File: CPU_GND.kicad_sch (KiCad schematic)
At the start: 1 part

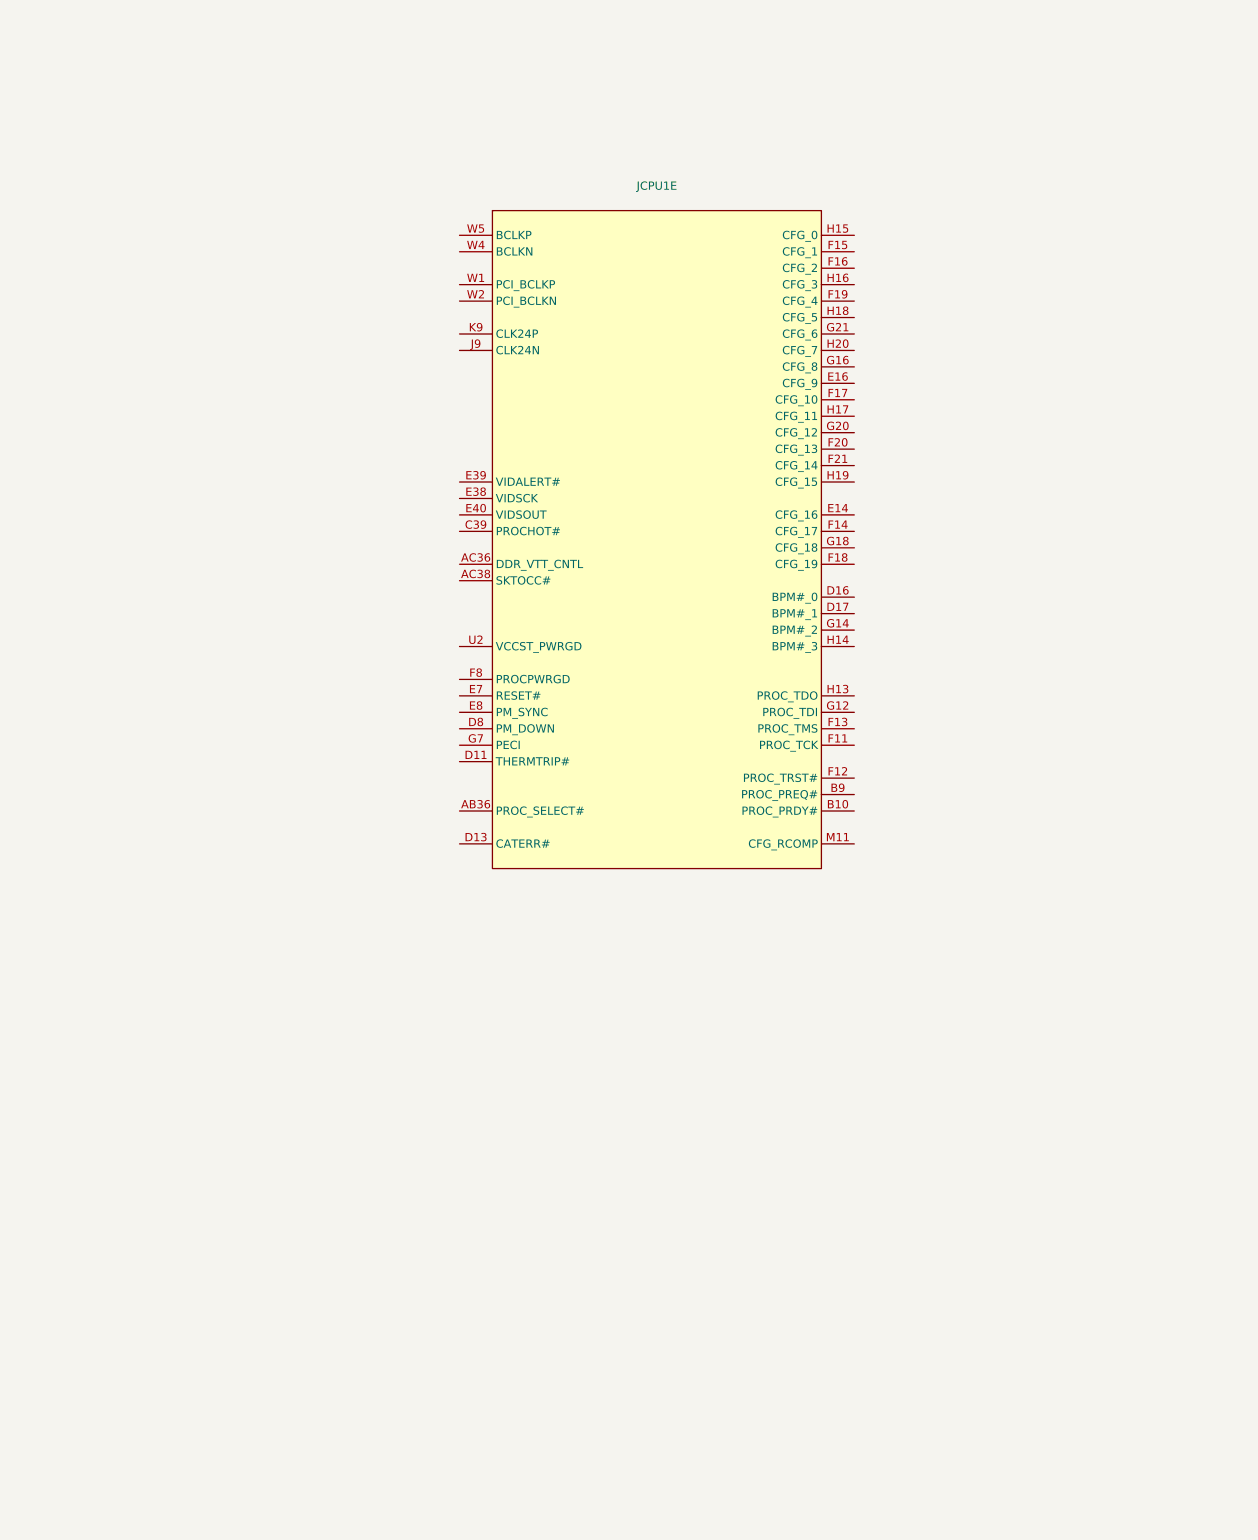
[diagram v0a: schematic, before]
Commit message: Added CPU GND and Core VCC symbols
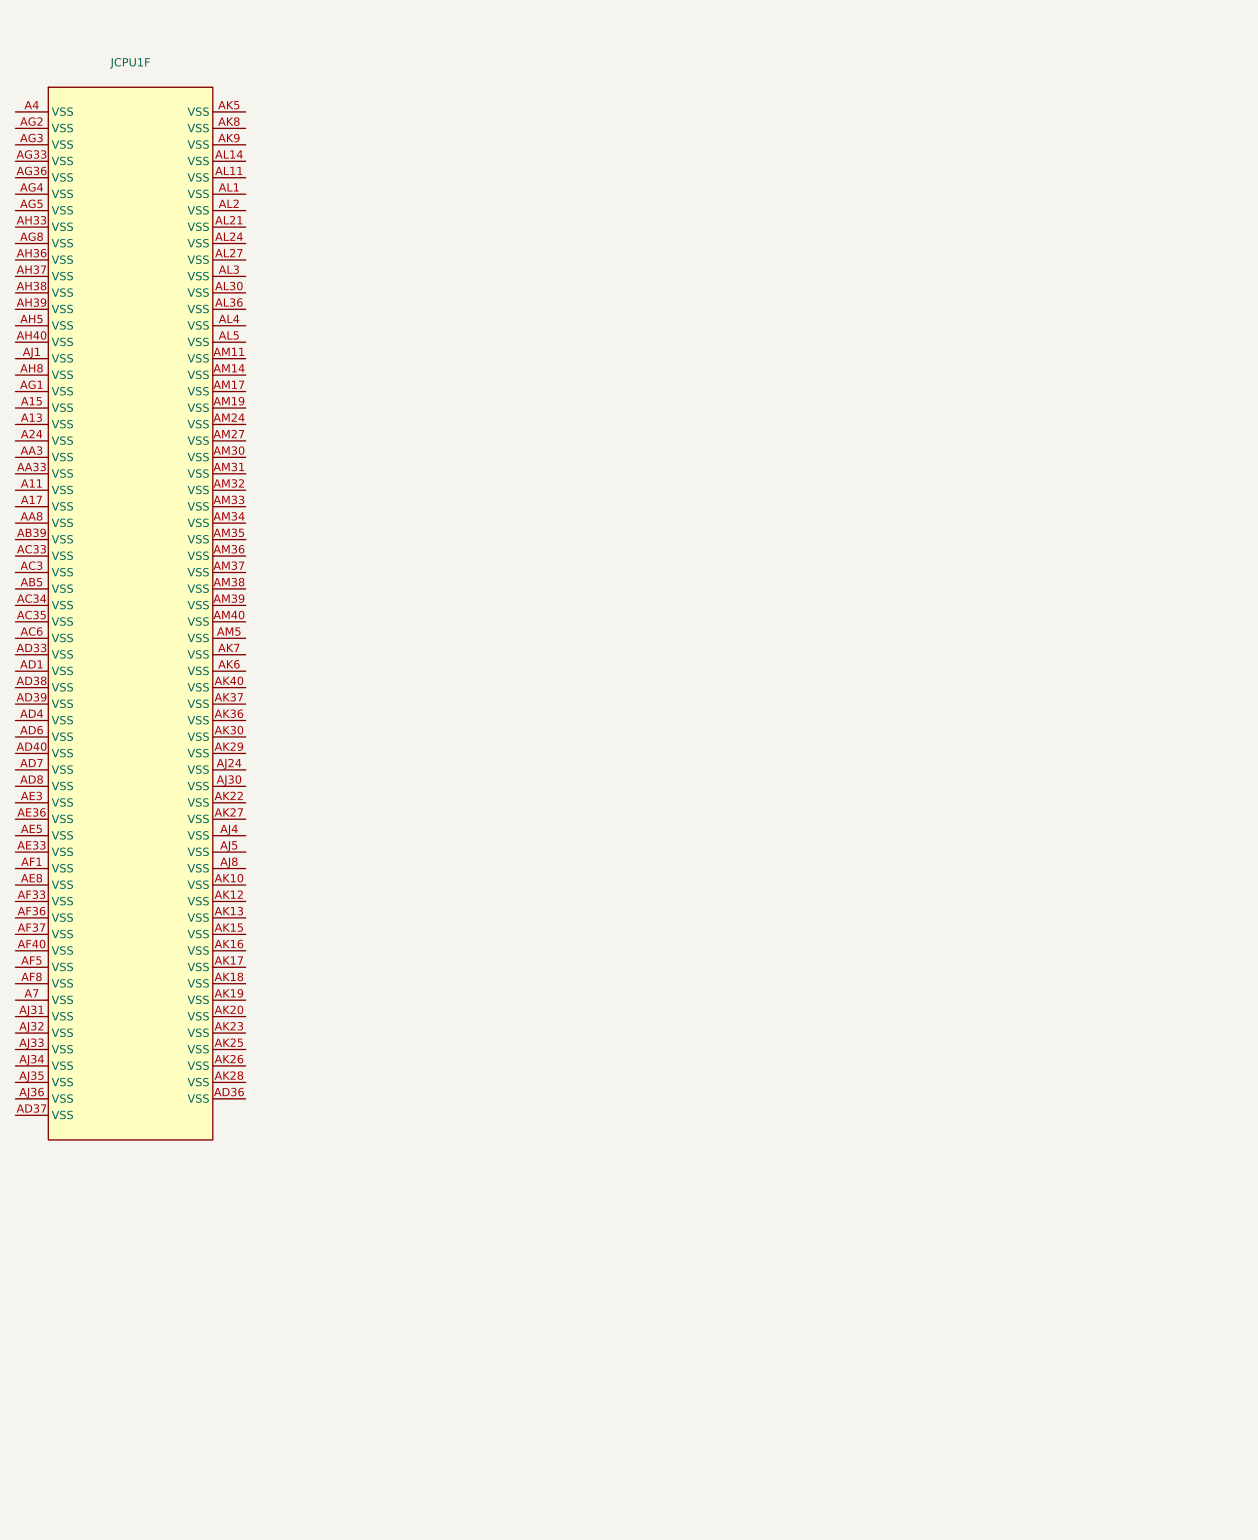
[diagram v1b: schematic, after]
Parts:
- removed JCPU1: ~, A-my-stuff:LGA-1151_L47.1-W42.5-P0.91_PE115127-4041-01H, symbol A-my-stuff:Intel_CFL_1151
- added JCPU1: ~, A-my-stuff:LGA-1151_L47.1-W42.5-P0.91_PE115127-4041-01H, symbol A-my-stuff:Intel_CFL_1151
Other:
- title: CPU Clock, CFG, VID & JTAG -> CPU Ground

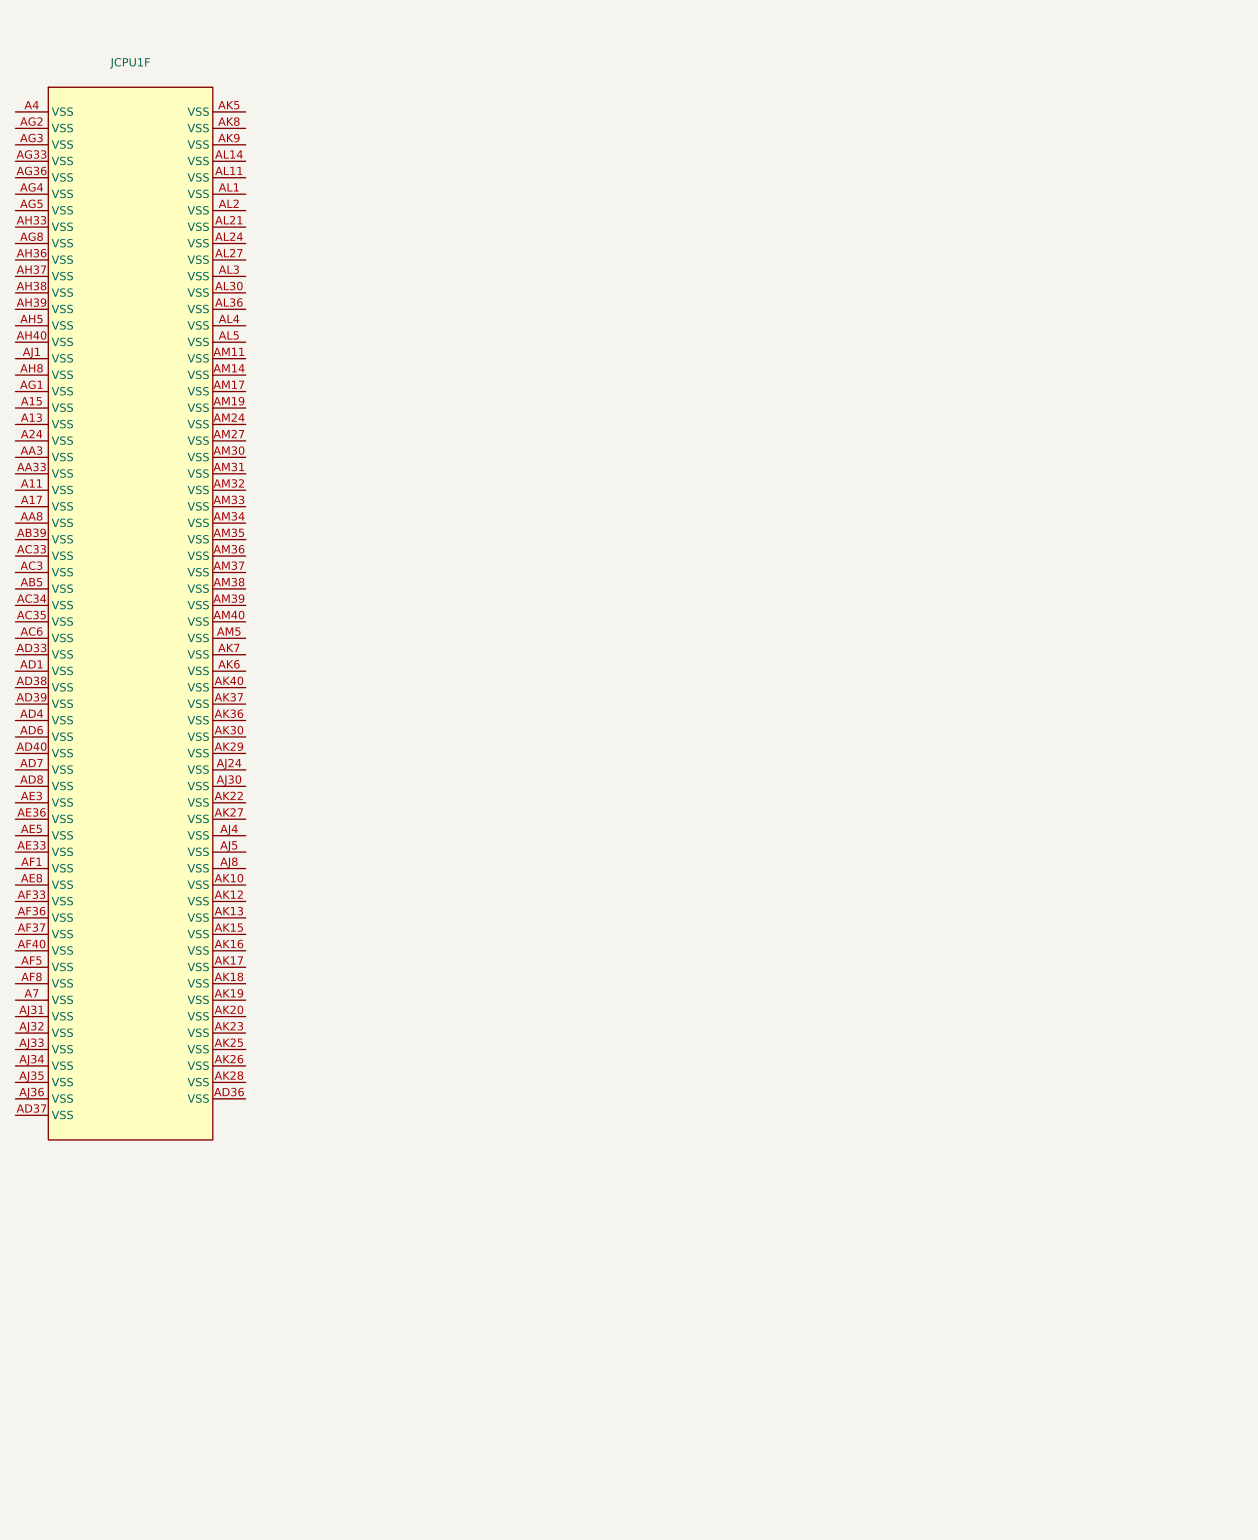
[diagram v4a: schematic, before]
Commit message: Added the last 2 CPU Ground symbols, CPU symbol set complete
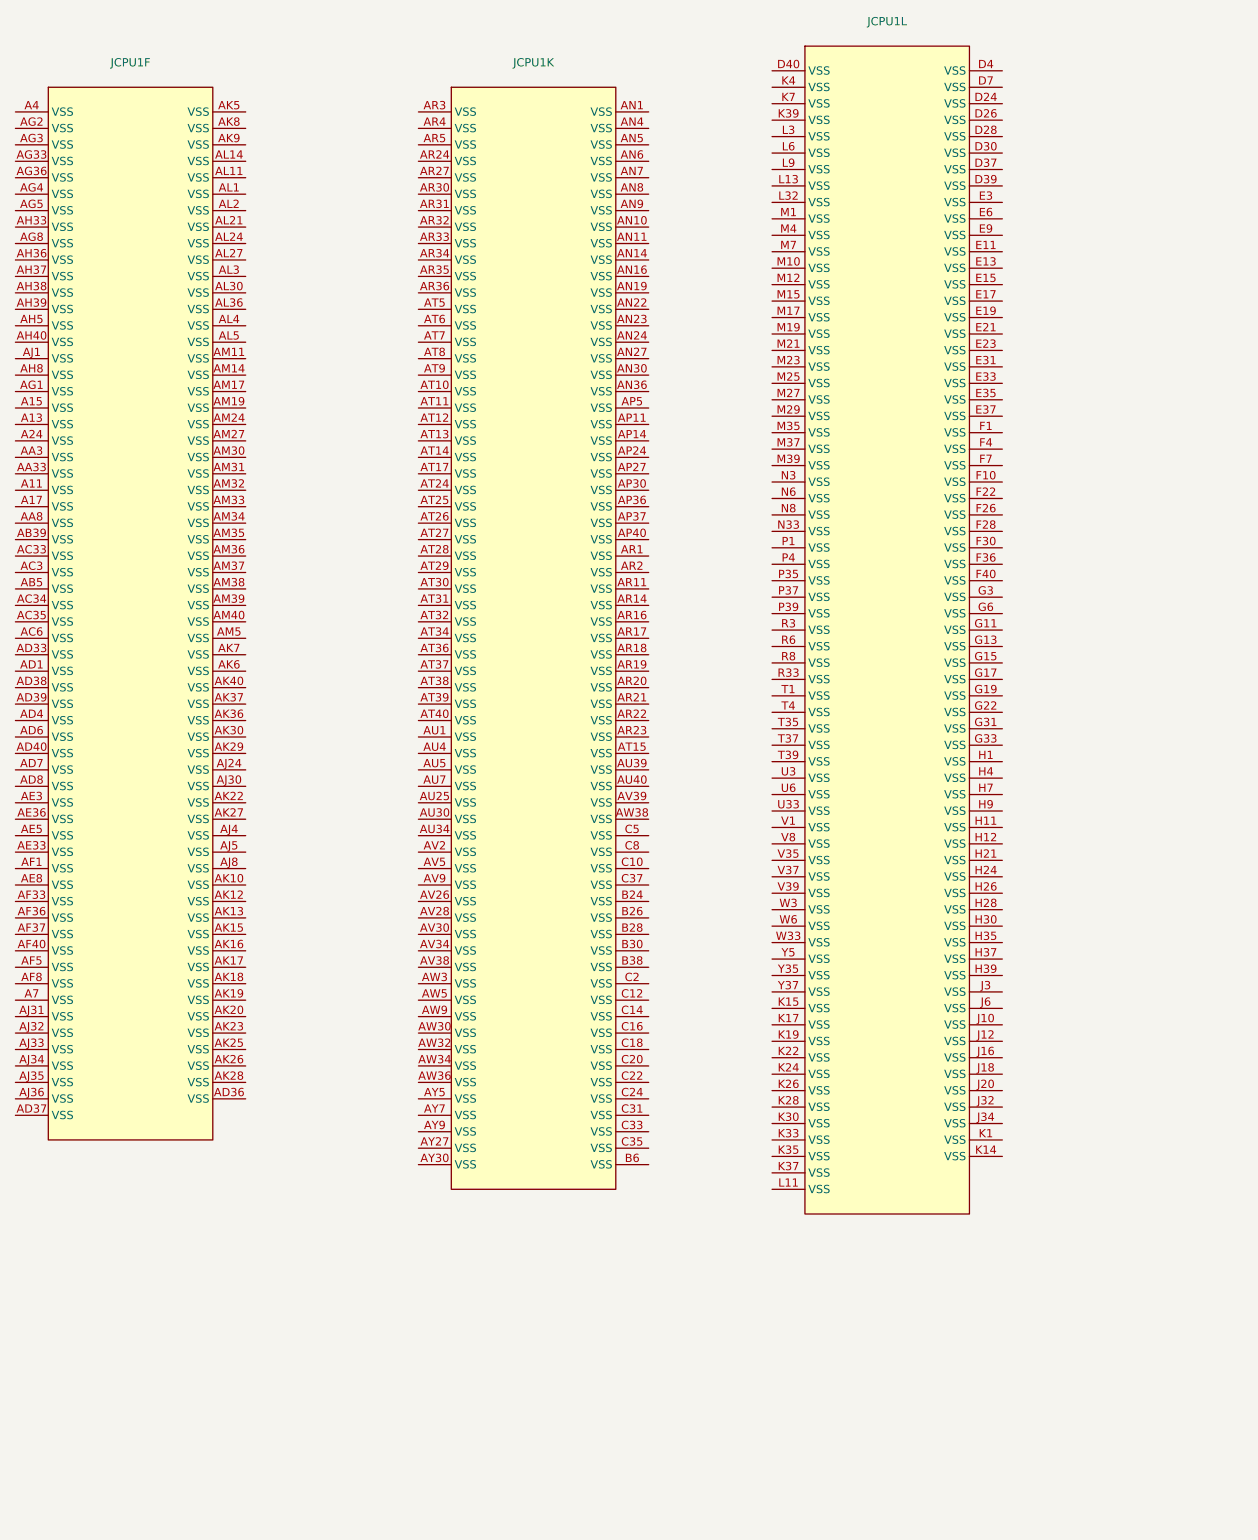
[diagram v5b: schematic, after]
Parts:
- added unit 12 of JCPU1
- added unit 11 of JCPU1

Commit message: Connected CPU ground
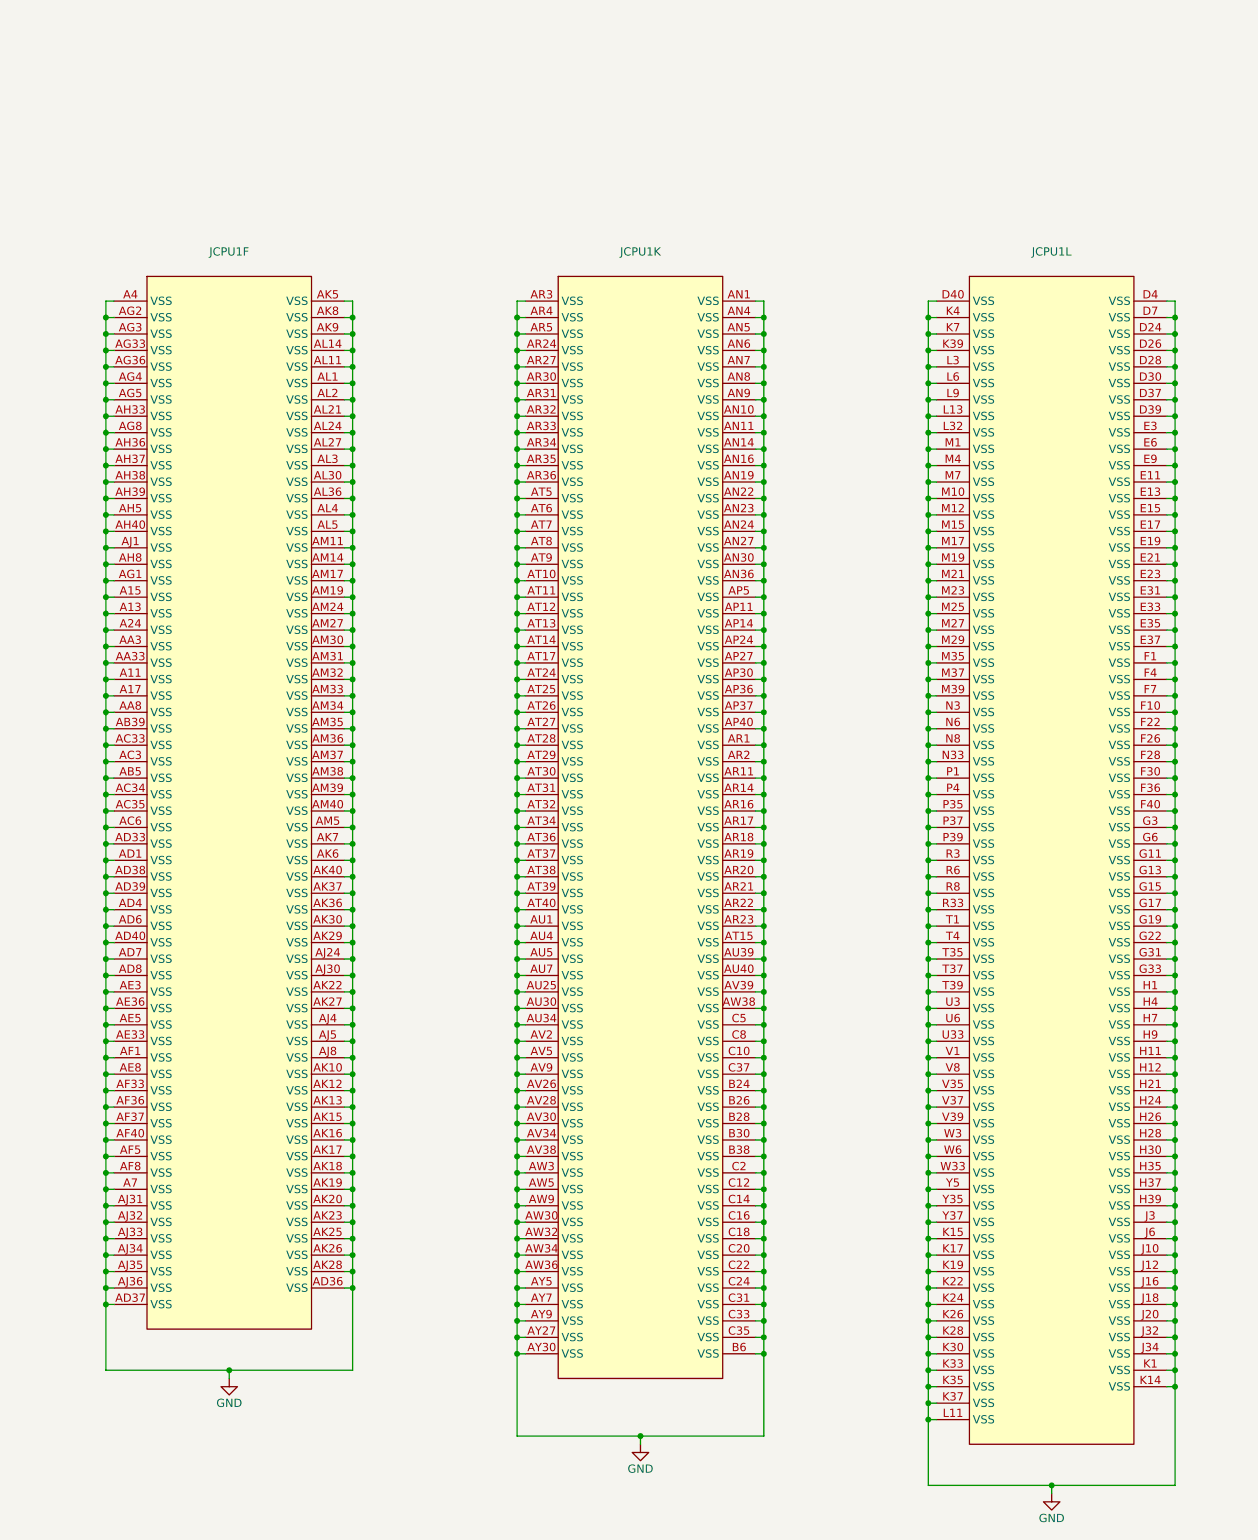
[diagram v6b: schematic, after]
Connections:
- net GND: now reaches JCPU1.D24 (VSS)
- net GND: now also JCPU1.A11 (VSS), JCPU1.A13 (VSS), JCPU1.A15 (VSS), JCPU1.A17 (VSS), JCPU1.A24 (VSS), JCPU1.A4 (VSS), JCPU1.A7 (VSS), JCPU1.AA3 (VSS), JCPU1.AA33 (VSS), JCPU1.AA8 (VSS), JCPU1.AB39 (VSS), JCPU1.AB5 (VSS), JCPU1.AC3 (VSS), JCPU1.AC33 (VSS), JCPU1.AC34 (VSS), JCPU1.AC35 (VSS), JCPU1.AC6 (VSS), JCPU1.AD1 (VSS), JCPU1.AD33 (VSS), JCPU1.AD36 (VSS), JCPU1.AD37 (VSS), JCPU1.AD38 (VSS), JCPU1.AD39 (VSS), JCPU1.AD4 (VSS), JCPU1.AD40 (VSS), JCPU1.AD6 (VSS), JCPU1.AD7 (VSS), JCPU1.AD8 (VSS), JCPU1.AE3 (VSS), JCPU1.AE33 (VSS), JCPU1.AE36 (VSS), JCPU1.AE5 (VSS), JCPU1.AE8 (VSS), JCPU1.AF1 (VSS), JCPU1.AF33 (VSS), JCPU1.AF36 (VSS), JCPU1.AF37 (VSS), JCPU1.AF40 (VSS), JCPU1.AF5 (VSS), JCPU1.AF8 (VSS), JCPU1.AG1 (VSS), JCPU1.AG2 (VSS), JCPU1.AG3 (VSS), JCPU1.AG33 (VSS), JCPU1.AG36 (VSS), JCPU1.AG4 (VSS), JCPU1.AG5 (VSS), JCPU1.AG8 (VSS), JCPU1.AH33 (VSS), JCPU1.AH36 (VSS), JCPU1.AH37 (VSS), JCPU1.AH38 (VSS), JCPU1.AH39 (VSS), JCPU1.AH40 (VSS), JCPU1.AH5 (VSS), JCPU1.AH8 (VSS), JCPU1.AJ1 (VSS), JCPU1.AJ24 (VSS), JCPU1.AJ30 (VSS), JCPU1.AJ31 (VSS), JCPU1.AJ32 (VSS), JCPU1.AJ33 (VSS), JCPU1.AJ34 (VSS), JCPU1.AJ35 (VSS), JCPU1.AJ36 (VSS), JCPU1.AJ4 (VSS), JCPU1.AJ5 (VSS), JCPU1.AJ8 (VSS), JCPU1.AK10 (VSS), JCPU1.AK12 (VSS), JCPU1.AK13 (VSS), JCPU1.AK15 (VSS), JCPU1.AK16 (VSS), JCPU1.AK17 (VSS), JCPU1.AK18 (VSS), JCPU1.AK19 (VSS), JCPU1.AK20 (VSS), JCPU1.AK22 (VSS), JCPU1.AK23 (VSS), JCPU1.AK25 (VSS), JCPU1.AK26 (VSS), JCPU1.AK27 (VSS), JCPU1.AK28 (VSS), JCPU1.AK29 (VSS), JCPU1.AK30 (VSS), JCPU1.AK36 (VSS), JCPU1.AK37 (VSS), JCPU1.AK40 (VSS), JCPU1.AK5 (VSS), JCPU1.AK6 (VSS), JCPU1.AK7 (VSS), JCPU1.AK8 (VSS), JCPU1.AK9 (VSS), JCPU1.AL1 (VSS), JCPU1.AL11 (VSS), JCPU1.AL14 (VSS), JCPU1.AL2 (VSS), JCPU1.AL21 (VSS), JCPU1.AL24 (VSS), JCPU1.AL27 (VSS), JCPU1.AL3 (VSS), JCPU1.AL30 (VSS), JCPU1.AL36 (VSS), JCPU1.AL4 (VSS), JCPU1.AL5 (VSS), JCPU1.AM11 (VSS), JCPU1.AM14 (VSS), JCPU1.AM17 (VSS), JCPU1.AM19 (VSS), JCPU1.AM24 (VSS), JCPU1.AM27 (VSS), JCPU1.AM30 (VSS), JCPU1.AM31 (VSS), JCPU1.AM32 (VSS), JCPU1.AM33 (VSS), JCPU1.AM34 (VSS), JCPU1.AM35 (VSS), JCPU1.AM36 (VSS), JCPU1.AM37 (VSS), JCPU1.AM38 (VSS), JCPU1.AM39 (VSS), JCPU1.AM40 (VSS), JCPU1.AM5 (VSS), JCPU1.AN1 (VSS), JCPU1.AN10 (VSS), JCPU1.AN11 (VSS), JCPU1.AN14 (VSS), JCPU1.AN16 (VSS), JCPU1.AN19 (VSS), JCPU1.AN22 (VSS), JCPU1.AN23 (VSS), JCPU1.AN24 (VSS), JCPU1.AN27 (VSS), JCPU1.AN30 (VSS), JCPU1.AN36 (VSS), JCPU1.AN4 (VSS), JCPU1.AN5 (VSS), JCPU1.AN6 (VSS), JCPU1.AN7 (VSS), JCPU1.AN8 (VSS), JCPU1.AN9 (VSS), JCPU1.AP11 (VSS), JCPU1.AP14 (VSS), JCPU1.AP24 (VSS), JCPU1.AP27 (VSS), JCPU1.AP30 (VSS), JCPU1.AP36 (VSS), JCPU1.AP37 (VSS), JCPU1.AP40 (VSS), JCPU1.AP5 (VSS), JCPU1.AR1 (VSS), JCPU1.AR11 (VSS), JCPU1.AR14 (VSS), JCPU1.AR16 (VSS), JCPU1.AR17 (VSS), JCPU1.AR18 (VSS), JCPU1.AR19 (VSS), JCPU1.AR2 (VSS), JCPU1.AR20 (VSS), JCPU1.AR21 (VSS), JCPU1.AR22 (VSS), JCPU1.AR23 (VSS), JCPU1.AR24 (VSS), JCPU1.AR27 (VSS), JCPU1.AR3 (VSS), JCPU1.AR30 (VSS), JCPU1.AR31 (VSS), JCPU1.AR32 (VSS), JCPU1.AR33 (VSS), JCPU1.AR34 (VSS), JCPU1.AR35 (VSS), JCPU1.AR36 (VSS), JCPU1.AR4 (VSS), JCPU1.AR5 (VSS), JCPU1.AT10 (VSS), JCPU1.AT11 (VSS), JCPU1.AT12 (VSS), JCPU1.AT13 (VSS), JCPU1.AT14 (VSS), JCPU1.AT15 (VSS), JCPU1.AT17 (VSS), JCPU1.AT24 (VSS), JCPU1.AT25 (VSS), JCPU1.AT26 (VSS), JCPU1.AT27 (VSS), JCPU1.AT28 (VSS), JCPU1.AT29 (VSS), JCPU1.AT30 (VSS), JCPU1.AT31 (VSS), JCPU1.AT32 (VSS), JCPU1.AT34 (VSS), JCPU1.AT36 (VSS), JCPU1.AT37 (VSS), JCPU1.AT38 (VSS), JCPU1.AT39 (VSS), JCPU1.AT40 (VSS), JCPU1.AT5 (VSS), JCPU1.AT6 (VSS), JCPU1.AT7 (VSS), JCPU1.AT8 (VSS), JCPU1.AT9 (VSS), JCPU1.AU1 (VSS), JCPU1.AU25 (VSS), JCPU1.AU30 (VSS), JCPU1.AU34 (VSS), JCPU1.AU39 (VSS), JCPU1.AU4 (VSS), JCPU1.AU40 (VSS), JCPU1.AU5 (VSS), JCPU1.AU7 (VSS), JCPU1.AV2 (VSS), JCPU1.AV26 (VSS), JCPU1.AV28 (VSS), JCPU1.AV30 (VSS), JCPU1.AV34 (VSS), JCPU1.AV38 (VSS), JCPU1.AV39 (VSS), JCPU1.AV5 (VSS), JCPU1.AV9 (VSS), JCPU1.AW3 (VSS), JCPU1.AW30 (VSS), JCPU1.AW32 (VSS), JCPU1.AW34 (VSS), JCPU1.AW36 (VSS), JCPU1.AW38 (VSS), JCPU1.AW5 (VSS), JCPU1.AW9 (VSS), JCPU1.AY27 (VSS), JCPU1.AY30 (VSS), JCPU1.AY5 (VSS), JCPU1.AY7 (VSS), JCPU1.AY9 (VSS), JCPU1.B24 (VSS), JCPU1.B26 (VSS), JCPU1.B28 (VSS), JCPU1.B30 (VSS), JCPU1.B38 (VSS), JCPU1.B6 (VSS), JCPU1.C10 (VSS), JCPU1.C12 (VSS), JCPU1.C14 (VSS), JCPU1.C16 (VSS), JCPU1.C18 (VSS), JCPU1.C2 (VSS), JCPU1.C20 (VSS), JCPU1.C22 (VSS), JCPU1.C24 (VSS), JCPU1.C31 (VSS), JCPU1.C33 (VSS), JCPU1.C35 (VSS), JCPU1.C37 (VSS), JCPU1.C5 (VSS), JCPU1.C8 (VSS), JCPU1.D26 (VSS), JCPU1.D28 (VSS), JCPU1.D30 (VSS), JCPU1.D37 (VSS), JCPU1.D39 (VSS), JCPU1.D4 (VSS), JCPU1.D40 (VSS), JCPU1.D7 (VSS), JCPU1.E11 (VSS), JCPU1.E13 (VSS), JCPU1.E15 (VSS), JCPU1.E17 (VSS), JCPU1.E19 (VSS), JCPU1.E21 (VSS), JCPU1.E23 (VSS), JCPU1.E3 (VSS), JCPU1.E31 (VSS), JCPU1.E33 (VSS), JCPU1.E35 (VSS), JCPU1.E37 (VSS), JCPU1.E6 (VSS), JCPU1.E9 (VSS), JCPU1.F1 (VSS), JCPU1.F10 (VSS), JCPU1.F22 (VSS), JCPU1.F26 (VSS), JCPU1.F28 (VSS), JCPU1.F30 (VSS), JCPU1.F36 (VSS), JCPU1.F4 (VSS), JCPU1.F40 (VSS), JCPU1.F7 (VSS), JCPU1.G11 (VSS), JCPU1.G13 (VSS), JCPU1.G15 (VSS), JCPU1.G17 (VSS), JCPU1.G19 (VSS), JCPU1.G22 (VSS), JCPU1.G3 (VSS), JCPU1.G31 (VSS), JCPU1.G33 (VSS), JCPU1.G6 (VSS), JCPU1.H1 (VSS), JCPU1.H11 (VSS), JCPU1.H12 (VSS), JCPU1.H21 (VSS), JCPU1.H24 (VSS), JCPU1.H26 (VSS), JCPU1.H28 (VSS), JCPU1.H30 (VSS), JCPU1.H35 (VSS), JCPU1.H37 (VSS), JCPU1.H39 (VSS), JCPU1.H4 (VSS), JCPU1.H7 (VSS), JCPU1.H9 (VSS), JCPU1.J10 (VSS), JCPU1.J12 (VSS), JCPU1.J16 (VSS), JCPU1.J18 (VSS), JCPU1.J20 (VSS), JCPU1.J3 (VSS), JCPU1.J32 (VSS), JCPU1.J34 (VSS), JCPU1.J6 (VSS), JCPU1.K1 (VSS), JCPU1.K14 (VSS), JCPU1.K15 (VSS), JCPU1.K17 (VSS), JCPU1.K19 (VSS), JCPU1.K22 (VSS), JCPU1.K24 (VSS), JCPU1.K26 (VSS), JCPU1.K28 (VSS), JCPU1.K30 (VSS), JCPU1.K33 (VSS), JCPU1.K35 (VSS), JCPU1.K37 (VSS), JCPU1.K39 (VSS), JCPU1.K4 (VSS), JCPU1.K7 (VSS), JCPU1.L11 (VSS), JCPU1.L13 (VSS), JCPU1.L3 (VSS), JCPU1.L32 (VSS), JCPU1.L6 (VSS), JCPU1.L9 (VSS), JCPU1.M1 (VSS), JCPU1.M10 (VSS), JCPU1.M12 (VSS), JCPU1.M15 (VSS), JCPU1.M17 (VSS), JCPU1.M19 (VSS), JCPU1.M21 (VSS), JCPU1.M23 (VSS), JCPU1.M25 (VSS), JCPU1.M27 (VSS), JCPU1.M29 (VSS), JCPU1.M35 (VSS), JCPU1.M37 (VSS), JCPU1.M39 (VSS), JCPU1.M4 (VSS), JCPU1.M7 (VSS), JCPU1.N3 (VSS), JCPU1.N33 (VSS), JCPU1.N6 (VSS), JCPU1.N8 (VSS), JCPU1.P1 (VSS), JCPU1.P35 (VSS), JCPU1.P37 (VSS), JCPU1.P39 (VSS), JCPU1.P4 (VSS), JCPU1.R3 (VSS), JCPU1.R33 (VSS), JCPU1.R6 (VSS), JCPU1.R8 (VSS), JCPU1.T1 (VSS), JCPU1.T35 (VSS), JCPU1.T37 (VSS), JCPU1.T39 (VSS), JCPU1.T4 (VSS), JCPU1.U3 (VSS), JCPU1.U33 (VSS), JCPU1.U6 (VSS), JCPU1.V1 (VSS), JCPU1.V35 (VSS), JCPU1.V37 (VSS), JCPU1.V39 (VSS), JCPU1.V8 (VSS), JCPU1.W3 (VSS), JCPU1.W33 (VSS), JCPU1.W6 (VSS), JCPU1.Y35 (VSS), JCPU1.Y37 (VSS), JCPU1.Y5 (VSS)
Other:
- moved on the sheet: JCPU1F, JCPU1K, JCPU1L

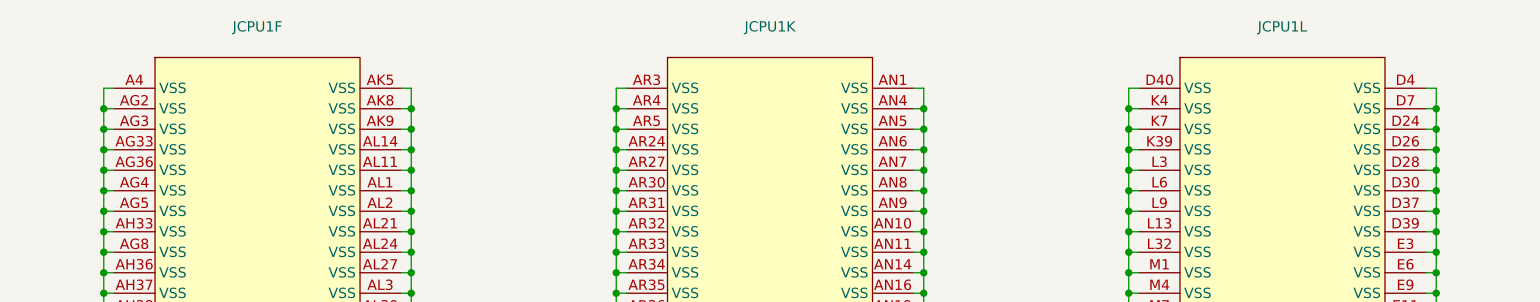
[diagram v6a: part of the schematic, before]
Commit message: Added first PCH symbol and footprint
THANKS @mothenjoyer69 so much for extracting and converting the PCH footprint from a laptop boardview ❤️
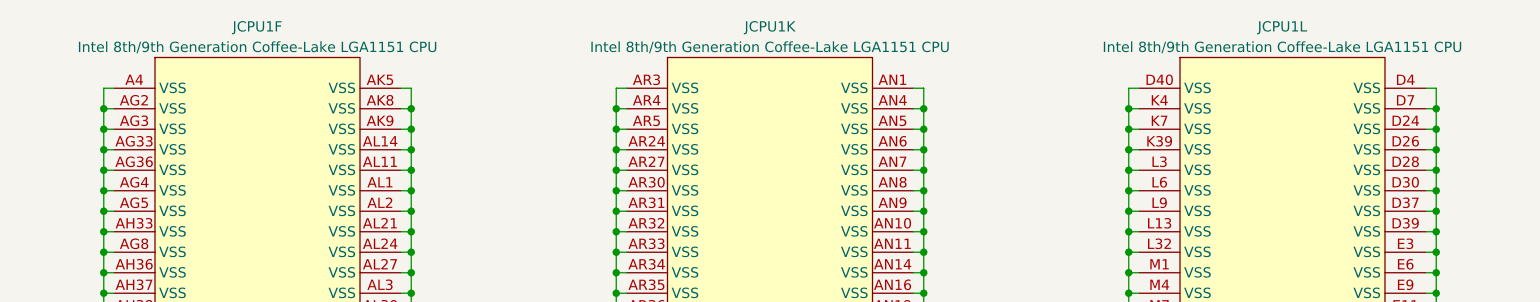
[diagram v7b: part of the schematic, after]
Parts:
- JCPU1: value ~ -> Intel 8th/9th Generation Coffee-Lake LGA1151 CPU
